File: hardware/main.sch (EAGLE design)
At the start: 28 parts, among them IC3 E73_2G4M04S, J3 DCJ0202, J4 SCREWTERMINAL_3X, Q1 BUZ11, Q2 BUZ11, Q3 BUZ11, Q4 BUZ11

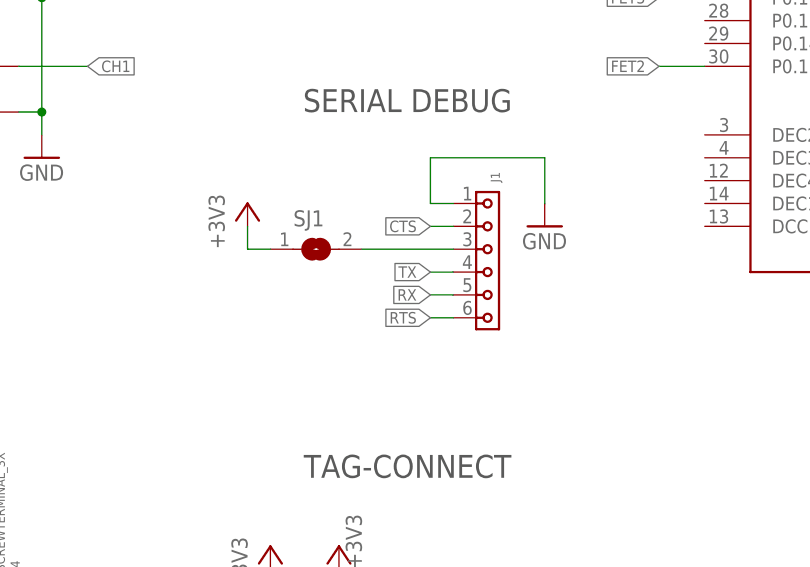
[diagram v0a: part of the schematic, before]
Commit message: enhanced Readme after testing
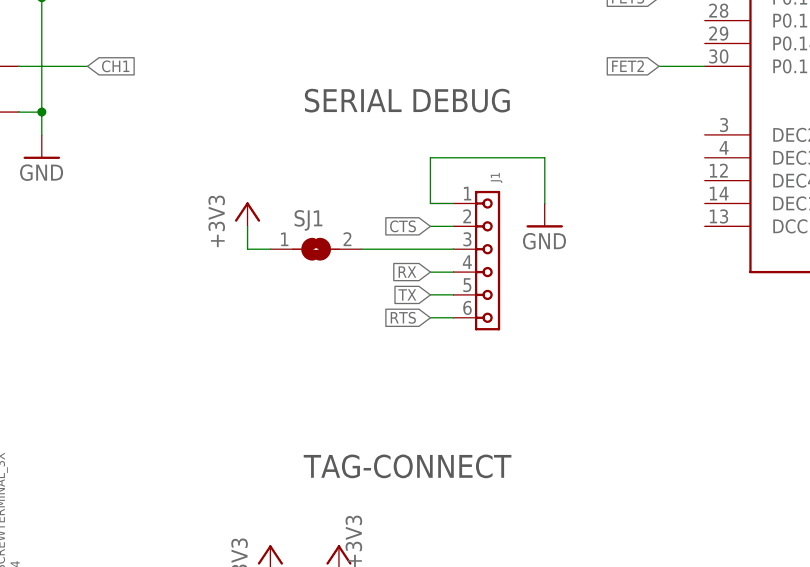
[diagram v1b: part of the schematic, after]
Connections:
- net RX: now also J1.4; no longer J1.5
- net TX: now also J1.5; no longer J1.4
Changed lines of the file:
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@@
 </segment>
 <segment>
-<pinref part="J1" gate="G$1" pin="4"/>
-<wire x1="106.68" y1="86.36" x2="104.14" y2="86.36" width="0.1524" layer="91"/>
-<label x="104.14" y="86.36" size="1.27" layer="95" rot="R180" xref="yes"/>
+<wire x1="106.68" y1="83.82" x2="104.14" y2="83.82" width="0.1524" layer="91"/>
+<label x="104.14" y="83.82" size="1.27" layer="95" rot="R180" xref="yes"/>
+<pinref part="J1" gate="G$1" pin="5"/>
 </segment>
 </net>
@@
 </segment>
 <segment>
-<pinref part="J1" gate="G$1" pin="5"/>
-<wire x1="106.68" y1="83.82" x2="104.14" y2="83.82" width="0.1524" layer="91"/>
-<label x="104.14" y="83.82" size="1.27" layer="95" rot="R180" xref="yes"/>
+<wire x1="106.68" y1="86.36" x2="104.14" y2="86.36" width="0.1524" layer="91"/>
+<label x="104.14" y="86.36" size="1.27" layer="95" rot="R180" xref="yes"/>
+<pinref part="J1" gate="G$1" pin="4"/>
 </segment>
 </net>
